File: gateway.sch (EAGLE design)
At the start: 68 parts, among them J1 RASPBERRYPI-40-PIN-GPIO_PTH_N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, Q1 BSS123

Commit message: added reset for IMU
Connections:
- net GPIO5: now also U$4.RST
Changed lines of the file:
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@@
 <label x="266.7" y="231.14" size="1.778" layer="95"/>
+</segment>
+<segment>
+<pinref part="U$4" gate="G$1" pin="RST"/>
+<wire x1="276.86" y1="152.4" x2="269.24" y2="152.4" width="0.1524" layer="91"/>
 </segment>
 </net>

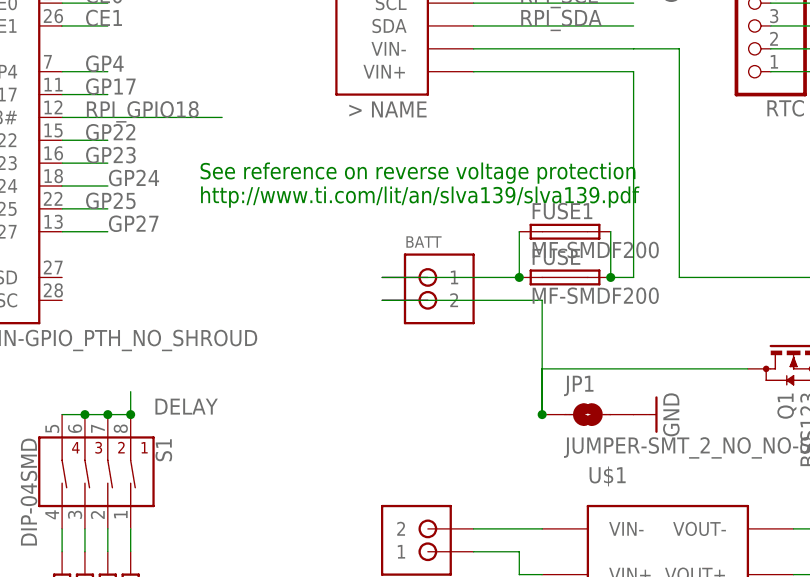
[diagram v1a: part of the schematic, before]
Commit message: added header for main_switch
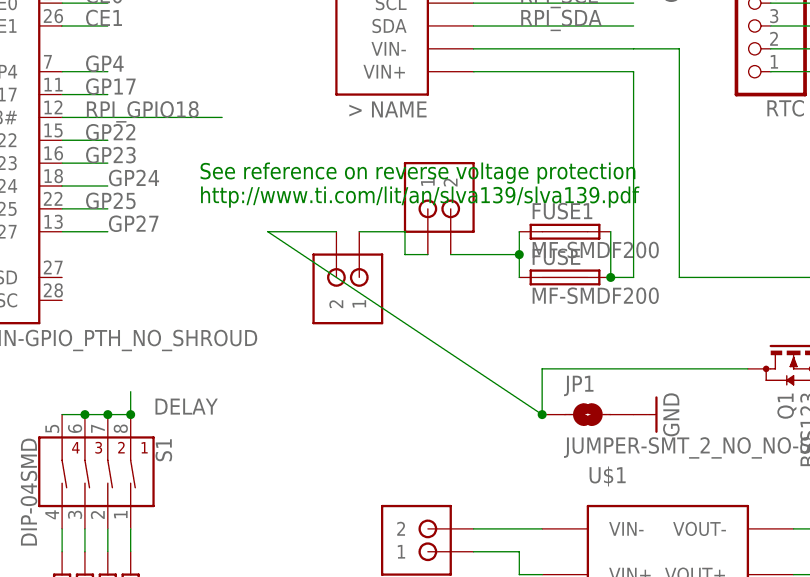
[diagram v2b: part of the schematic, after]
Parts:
- added MAIN_SWITCH: JST-PH_2-PIN_HEADER, SRG:JST-PH_2-PIN_HEADER
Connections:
- new net N$13: BATT.1, MAIN_SWITCH.1
- net BATT+: now also MAIN_SWITCH.2; no longer BATT.1
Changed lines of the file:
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@@
 <part name="C4" library="rcl" deviceset="C-US" device="C1812"/>
 <part name="RAIN" library="jst" deviceset="B3B-ZR" device=""/>
+<part name="MAIN_SWITCH" library="SRG" deviceset="JST-PH_2-PIN_HEADER" device=""/>
 </parts>
 <sheets>
@@
 <instance part="RPI_VIN" gate="G$1" x="226.06" y="96.52" rot="R180"/>
 <instance part="GND11" gate="1" x="236.22" y="55.88"/>
-<instance part="BATT" gate="G$1" x="160.02" y="66.04" smashed="yes">
-<attribute name="NAME" x="154.94" y="71.882" size="1.27" layer="95" font="vector"/>
-</instance>
+<instance part="BATT" gate="G$1" x="147.32" y="66.04" smashed="yes" rot="R270"/>
 <instance part="INA219" gate="G$1" x="157.48" y="96.52" smashed="yes" rot="MR0"/>
 <instance part="PCB2" gate="G$1" x="5.08" y="170.18" rot="R270"/>
@@
 <instance part="C4" gate="G$1" x="320.04" y="215.9"/>
 <instance part="RAIN" gate="G$1" x="246.38" y="127" rot="R180"/>
+<instance part="MAIN_SWITCH" gate="G$1" x="160.02" y="78.74" smashed="yes" rot="R90"/>
 </instances>
 <busses>
@@
 </segment>
 <segment>
-<pinref part="BATT" gate="G$1" pin="1"/>
 <pinref part="FUSE" gate="A" pin="1"/>
-<wire x1="152.4" y1="68.58" x2="167.64" y2="68.58" width="0.1524" layer="91"/>
 <pinref part="FUSE1" gate="A" pin="1"/>
-<wire x1="167.64" y1="73.66" x2="167.64" y2="68.58" width="0.1524" layer="91"/>
-<junction x="167.64" y="68.58"/>
+<wire x1="167.64" y1="73.66" x2="167.64" y2="71.12" width="0.1524" layer="91"/>
+<pinref part="MAIN_SWITCH" gate="G$1" pin="2"/>
+<wire x1="167.64" y1="71.12" x2="167.64" y2="68.58" width="0.1524" layer="91"/>
+<wire x1="160.02" y1="71.12" x2="167.64" y2="71.12" width="0.1524" layer="91"/>
+<junction x="167.64" y="71.12"/>
 </segment>
 </net>
@@
 <wire x1="193.04" y1="58.42" x2="170.18" y2="58.42" width="0.1524" layer="91"/>
 <wire x1="170.18" y1="58.42" x2="170.18" y2="53.34" width="0.1524" layer="91"/>
-<wire x1="170.18" y1="53.34" x2="170.18" y2="66.04" width="0.1524" layer="91"/>
+<wire x1="170.18" y1="53.34" x2="139.7" y2="73.66" width="0.1524" layer="91"/>
 <pinref part="JP1" gate="G$1" pin="1"/>
 <junction x="170.18" y="53.34"/>
 <pinref part="BATT" gate="G$1" pin="2"/>
-<wire x1="152.4" y1="66.04" x2="170.18" y2="66.04" width="0.1524" layer="91"/>
+<wire x1="147.32" y1="73.66" x2="139.7" y2="73.66" width="0.1524" layer="91"/>
 </segment>
 <segment>
@@
 </segment>
 </net>
+<net name="N$13" class="0">
+<segment>
+<pinref part="BATT" gate="G$1" pin="1"/>
+<wire x1="149.86" y1="73.66" x2="154.94" y2="73.66" width="0.1524" layer="91"/>
+<wire x1="154.94" y1="73.66" x2="154.94" y2="71.12" width="0.1524" layer="91"/>
+<pinref part="MAIN_SWITCH" gate="G$1" pin="1"/>
+<wire x1="154.94" y1="71.12" x2="157.48" y2="71.12" width="0.1524" layer="91"/>
+</segment>
+</net>

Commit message: added soms
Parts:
- added PAD41: WIREPADSMD1,27-254, wirepad:WIREPADSMD1,27-254
- added SOMS: B3B-ZR, jst:B3B-ZR
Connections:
- new net N$15: PAD41.P, SOMS.2
- net FEATHER_3.3V: now also SOMS.3
- net GND: now also SOMS.1
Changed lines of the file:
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@@
 <part name="RAIN" library="jst" deviceset="B3B-ZR" device=""/>
 <part name="MAIN_SWITCH" library="SRG" deviceset="JST-PH_2-PIN_HEADER" device=""/>
+<part name="SOMS" library="jst" deviceset="B3B-ZR" device=""/>
+<part name="PAD41" library="wirepad" deviceset="WIREPAD" device="SMD1,27-254" value="WIREPADSMD1,27-254"/>
 </parts>
 <sheets>
@@
 <instance part="RAIN" gate="G$1" x="246.38" y="127" rot="R180"/>
 <instance part="MAIN_SWITCH" gate="G$1" x="160.02" y="78.74" smashed="yes" rot="R90"/>
+<instance part="SOMS" gate="G$1" x="292.1" y="127" rot="R180"/>
+<instance part="PAD41" gate="G$1" x="322.58" y="127" smashed="yes" rot="R180">
+<attribute name="NAME" x="323.723" y="125.1458" size="1.778" layer="95" rot="R180"/>
+</instance>
 </instances>
 <busses>
@@
 <pinref part="RAIN" gate="G$1" pin="1"/>
 <wire x1="254" y1="124.46" x2="264.16" y2="124.46" width="0.1524" layer="91"/>
+</segment>
+<segment>
+<pinref part="SOMS" gate="G$1" pin="1"/>
+<wire x1="299.72" y1="124.46" x2="309.88" y2="124.46" width="0.1524" layer="91"/>
 </segment>
 </net>
@@
 <wire x1="276.86" y1="165.1" x2="264.16" y2="165.1" width="0.1524" layer="91"/>
 </segment>
+<segment>
+<pinref part="SOMS" gate="G$1" pin="3"/>
+<wire x1="299.72" y1="129.54" x2="309.88" y2="129.54" width="0.1524" layer="91"/>
+<label x="299.72" y="129.54" size="1.778" layer="95"/>
+</segment>
 </net>
 <net name="EN" class="0">
@@
 </segment>
 </net>
+<net name="N$15" class="0">
+<segment>
+<pinref part="SOMS" gate="G$1" pin="2"/>
+<wire x1="299.72" y1="127" x2="320.04" y2="127" width="0.1524" layer="91"/>
+<pinref part="PAD41" gate="G$1" pin="P"/>
+</segment>
+</net>

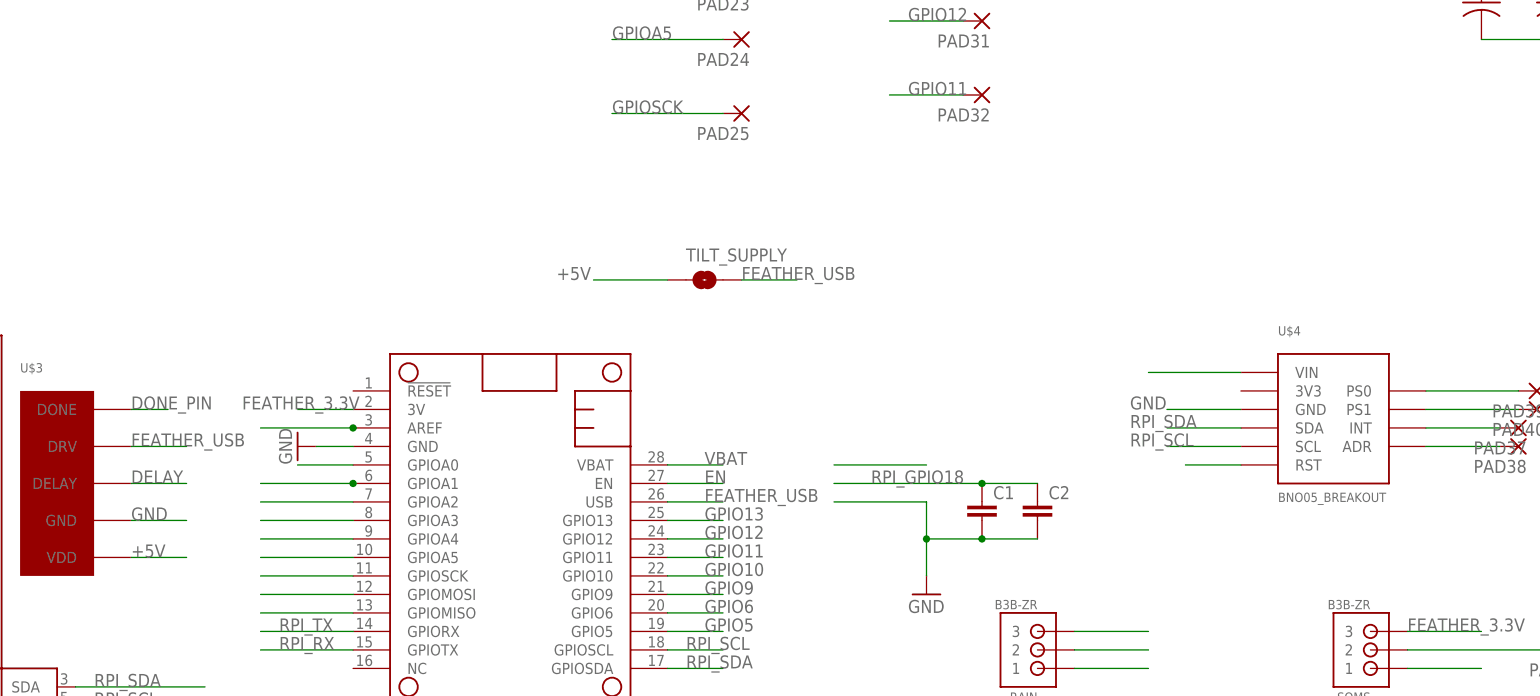
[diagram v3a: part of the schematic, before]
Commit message: Added a v2 for the tilt_soms_lgbu board (tilt_soms_lgbu_v2)
Primary changes:
Placed all components on top layer including the con-wago connectors.
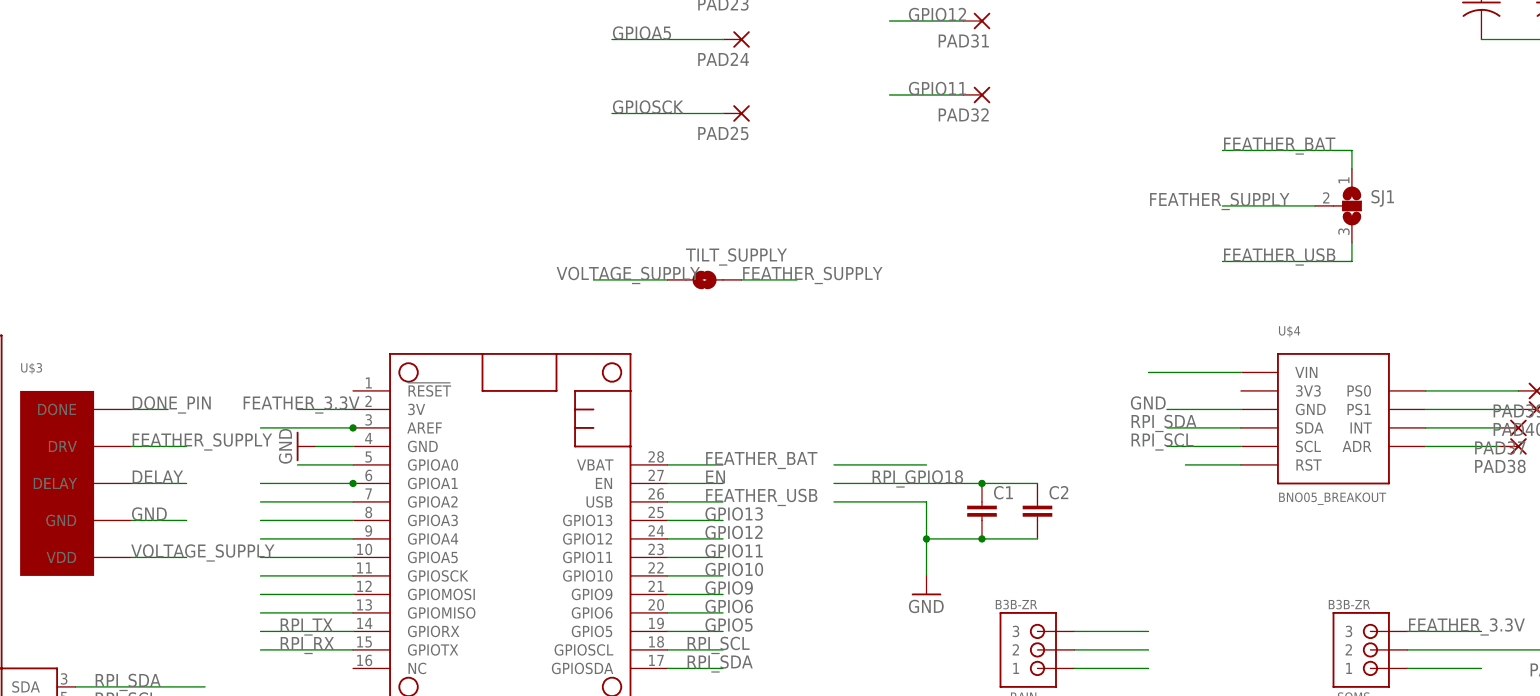
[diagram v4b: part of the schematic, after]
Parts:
- added SJ1: (no value), jumper:SJ2W
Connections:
- net +5V renamed VOLTAGE_SUPPLY
- new net FEATHER_BAT: MS1.VBAT, SJ1.1
- new net FEATHER_SUPPLY: SJ1.2, TILT_SUPPLY.2, U$3.DRV
- net FEATHER_USB: now also SJ1.3; no longer TILT_SUPPLY.2, U$3.DRV
- net VBAT: no longer MS1.VBAT
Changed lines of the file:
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@@
 <part name="SOMS" library="jst" deviceset="B3B-ZR" device=""/>
 <part name="PAD41" library="wirepad" deviceset="WIREPAD" device="SMD1,27-254" value="WIREPADSMD1,27-254"/>
+<part name="SJ1" library="jumper" deviceset="SJ2W" device=""/>
 </parts>
 <sheets>
@@
 <attribute name="NAME" x="323.723" y="125.1458" size="1.778" layer="95" rot="R180"/>
 </instance>
+<instance part="SJ1" gate="G$1" x="292.1" y="187.96"/>
 </instances>
 <busses>
@@
 </segment>
 </net>
-<net name="+5V" class="0">
+<net name="VOLTAGE_SUPPLY" class="0">
 <segment>
 <pinref part="P+1" gate="1" pin="+5V"/>
@@
 <net name="FEATHER_USB" class="0">
 <segment>
-<pinref part="TILT_SUPPLY" gate="G$1" pin="2"/>
-<wire x1="208.28" y1="177.8" x2="215.9" y2="177.8" width="0.1524" layer="91"/>
-<label x="208.28" y="177.8" size="1.778" layer="95"/>
-</segment>
-<segment>
 <pinref part="MS1" gate="G$1" pin="USB"/>
 <wire x1="198.12" y1="147.32" x2="205.74" y2="147.32" width="0.1524" layer="91"/>
@@
 </segment>
 <segment>
-<pinref part="U$3" gate="G$1" pin="DRV"/>
-<wire x1="124.46" y1="154.94" x2="132.08" y2="154.94" width="0.1524" layer="91"/>
-<label x="124.46" y="154.94" size="1.778" layer="95"/>
+<pinref part="SJ1" gate="G$1" pin="3"/>
+<wire x1="292.1" y1="182.88" x2="292.1" y2="180.34" width="0.1524" layer="91"/>
+<wire x1="292.1" y1="180.34" x2="274.32" y2="180.34" width="0.1524" layer="91"/>
+<label x="274.32" y="180.34" size="1.778" layer="95"/>
 </segment>
 </net>
@@
 </net>
 <net name="VBAT" class="0">
-<segment>
-<pinref part="MS1" gate="G$1" pin="VBAT"/>
-<wire x1="198.12" y1="152.4" x2="205.74" y2="152.4" width="0.1524" layer="91"/>
-<label x="203.2" y="152.4" size="1.778" layer="95"/>
-</segment>
 <segment>
 <pinref part="PAD28" gate="G$1" pin="P"/>
@@
 </segment>
 </net>
+<net name="FEATHER_SUPPLY" class="0">
+<segment>
+<pinref part="U$3" gate="G$1" pin="DRV"/>
+<wire x1="124.46" y1="154.94" x2="132.08" y2="154.94" width="0.1524" layer="91"/>
+<label x="124.46" y="154.94" size="1.778" layer="95"/>
+</segment>
+<segment>
+<pinref part="SJ1" gate="G$1" pin="2"/>
+<wire x1="287.02" y1="187.96" x2="274.32" y2="187.96" width="0.1524" layer="91"/>
+<label x="264.16" y="187.96" size="1.778" layer="95"/>
+</segment>
+<segment>
+<pinref part="TILT_SUPPLY" gate="G$1" pin="2"/>
+<wire x1="208.28" y1="177.8" x2="215.9" y2="177.8" width="0.1524" layer="91"/>
+<label x="208.28" y="177.8" size="1.778" layer="95"/>
+</segment>
+</net>
+<net name="FEATHER_BAT" class="0">
+<segment>
+<pinref part="SJ1" gate="G$1" pin="1"/>
+<wire x1="292.1" y1="193.04" x2="292.1" y2="195.58" width="0.1524" layer="91"/>
+<wire x1="292.1" y1="195.58" x2="274.32" y2="195.58" width="0.1524" layer="91"/>
+<label x="274.32" y="195.58" size="1.778" layer="95"/>
+</segment>
+<segment>
+<pinref part="MS1" gate="G$1" pin="VBAT"/>
+<wire x1="198.12" y1="152.4" x2="205.74" y2="152.4" width="0.1524" layer="91"/>
+<label x="203.2" y="152.4" size="1.778" layer="95"/>
+</segment>
+</net>
